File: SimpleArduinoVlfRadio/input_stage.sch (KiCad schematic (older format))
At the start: 0 parts

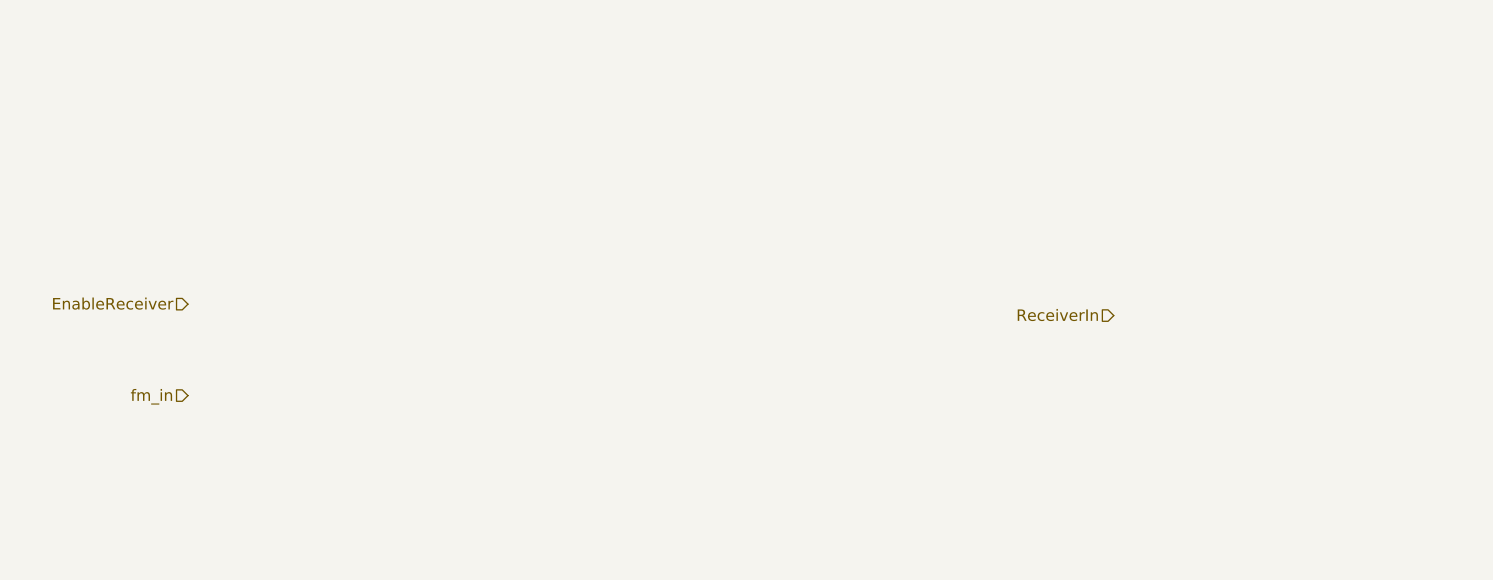
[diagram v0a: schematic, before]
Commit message: Updated Transmitter and finished fsk receiver
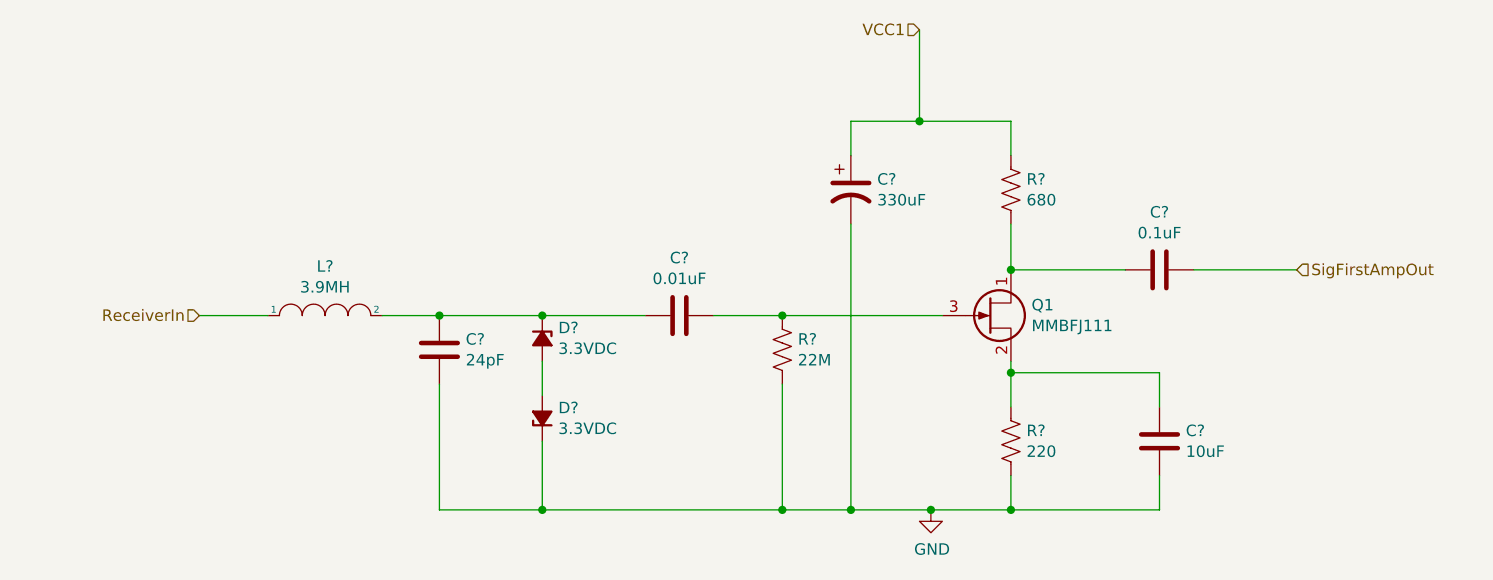
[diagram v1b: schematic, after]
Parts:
- added C?: 24pF, symbol Device:C
- added C?: 0.01uF, symbol Device:C
- added C?: 0.1uF, symbol Device:C
- added C?: 330uF, symbol Device:CP1
- added C?: 10uF, symbol Device:C
- added D? (x2): 3.3VDC, symbol Device:D_Zener_Small_ALT
- added L?: 3.9MH, symbol pspice:INDUCTOR
- added Q1: MMBFJ111, Package_TO_SOT_SMD:SOT-23, symbol Transistor_FET:MMBFJ111
- added R?: 22M, symbol Device:R_US
- added R?: 220, symbol Device:R_US
- added R?: 680, symbol Device:R_US
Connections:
- net ReceiverIn: now also L?.1
- new net: C?.2, Q1.1 (D), R?.2
- new net: C?.1, Q1.2 (S), R?.1
- new net: C?.1, Q1.3 (G), R?.1
- new net: C?.1, C?.2, D?.1 (K), L?.2
- new net: D?.2 (A), D?.2 (A)
- new net GND: C?.2, C?.2, C?.2, D?.1 (K), R?.2, R?.2
- new net SigFirstAmpOut: C?.1
- new net VCC1: C?.1, R?.1
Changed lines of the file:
@@
 $Descr A4 11693 8268
 encoding utf-8
-Sheet 5 10
+Sheet 7 14
 Title ""
 Date ""
@@
 Comment4 ""
 $EndDescr
-Text HLabel 2950 3100 0    50   Input ~ 0
-EnableReceiver
-Text HLabel 7000 3150 0    50   Input ~ 0
+Text HLabel 3000 3150 0    50   Input ~ 0
 ReceiverIn
-Text HLabel 2950 3500 0    50   Input ~ 0
-fm_in
+Text HLabel 7800 2950 2    50   Input ~ 0
+SigFirstAmpOut
+$Comp
+L Transistor_FET:MMBFJ111 Q1
+U 1 1 62A4F9A0
+P 6450 3150
+F 0 "Q1" H 6640 3196 50  0000 L CNN
+F 1 "MMBFJ111" H 6640 3105 50  0000 L CNN
+F 2 "Package_TO_SOT_SMD:SOT-23" H 6650 3075 50  0001 L CIN
+F 3 "https://www.onsemi.com/pub/Collateral/MMBFJ113-D.PDF" H 6450 3150 50  0001 L CNN
+	1    6450 3150
+	1    0    0    -1
+$EndComp
+$Comp
+L Device:D_Zener_Small_ALT D?
+U 1 1 62A51025
+P 4500 3250
+F 0 "D?" V 4454 3320 50  0000 L CNN
+F 1 "3.3VDC" V 4545 3320 50  0000 L CNN
+F 2 "" V 4500 3250 50  0001 C CNN
+F 3 "~" V 4500 3250 50  0001 C CNN
+	1    4500 3250
+	0    1    1    0
+$EndComp
+$Comp
+L Device:D_Zener_Small_ALT D?
+U 1 1 62A51E79
+P 4500 3600
+F 0 "D?" V 4546 3530 50  0000 R CNN
+F 1 "3.3VDC" V 4455 3530 50  0000 R CNN
+F 2 "" V 4500 3600 50  0001 C CNN
+F 3 "~" V 4500 3600 50  0001 C CNN
+	1    4500 3600
+	0    -1   -1   0
+$EndComp
+$Comp
+L Device:C C?
+U 1 1 62A52969
+P 4050 3300
+F 0 "C?" H 4165 3346 50  0000 L CNN
+F 1 "24pF" H 4165 3255 50  0000 L CNN
+F 2 "" H 4088 3150 50  0001 C CNN
+F 3 "~" H 4050 3300 50  0001 C CNN
+	1    4050 3300
+	1    0    0    -1
+$EndComp
+$Comp
+L pspice:INDUCTOR L?
+U 1 1 62A538F5
+P 3550 3150
+F 0 "L?" H 3550 3365 50  0000 C CNN
+F 1 "3.9MH" H 3550 3274 50  0000 C CNN
+F 2 "" H 3550 3150 50  0001 C CNN
+F 3 "~" H 3550 3150 50  0001 C CNN
+	1    3550 3150
+	1    0    0    -1
+$EndComp
+$Comp
+L Device:R_US R?
+U 1 1 62A55EF5
+P 5550 3300
+F 0 "R?" H 5618 3346 50  0000 L CNN
+F 1 "22M" H 5618 3255 50  0000 L CNN
+F 2 "" V 5590 3290 50  0001 C CNN
+F 3 "~" H 5550 3300 50  0001 C CNN
+	1    5550 3300
+	1    0    0    -1
+$EndComp
+$Comp
+L Device:R_US R?
+U 1 1 62A56EAC
+P 6550 3700
+F 0 "R?" H 6618 3746 50  0000 L CNN
+F 1 "220" H 6618 3655 50  0000 L CNN
+F 2 "" V 6590 3690 50  0001 C CNN
+F 3 "~" H 6550 3700 50  0001 C CNN
+	1    6550 3700
+	1    0    0    -1
+$EndComp
+$Comp
+L Device:R_US R?
+U 1 1 62A57945
+P 6550 2600
+F 0 "R?" H 6618 2646 50  0000 L CNN
+F 1 "680" H 6618 2555 50  0000 L CNN
+F 2 "" V 6590 2590 50  0001 C CNN
+F 3 "~" H 6550 2600 50  0001 C CNN
+	1    6550 2600
+	1    0    0    -1
+$EndComp
+$Comp
+L Device:C C?
+U 1 1 62A582F5
+P 5100 3150
+F 0 "C?" V 4848 3150 50  0000 C CNN
+F 1 "0.01uF" V 4939 3150 50  0000 C CNN
+F 2 "" H 5138 3000 50  0001 C CNN
+F 3 "~" H 5100 3150 50  0001 C CNN
+	1    5100 3150
+	0    1    1    0
+$EndComp
+$Comp
+L Device:C C?
+U 1 1 62A58A43
+P 7200 2950
+F 0 "C?" V 6948 2950 50  0000 C CNN
+F 1 "0.1uF" V 7039 2950 50  0000 C CNN
+F 2 "" H 7238 2800 50  0001 C CNN
+F 3 "~" H 7200 2950 50  0001 C CNN
+	1    7200 2950
+	0    1    1    0
+$EndComp
+$Comp
+L Device:CP1 C?
+U 1 1 62A5967F
+P 5850 2600
+F 0 "C?" H 5965 2646 50  0000 L CNN
+F 1 "330uF" H 5965 2555 50  0000 L CNN
+F 2 "" H 5850 2600 50  0001 C CNN
+F 3 "~" H 5850 2600 50  0001 C CNN
+	1    5850 2600
+	1    0    0    -1
+$EndComp
+$Comp
+L Device:C C?
+U 1 1 62A5ABDD
+P 7200 3700
+F 0 "C?" H 7315 3746 50  0000 L CNN
+F 1 "10uF" H 7315 3655 50  0000 L CNN
+F 2 "" H 7238 3550 50  0001 C CNN
+F 3 "~" H 7200 3700 50  0001 C CNN
+	1    7200 3700
+	1    0    0    -1
+$EndComp
+Wire Wire Line
+	3000 3150 3300 3150
+Wire Wire Line
+	3800 3150 4050 3150
+Wire Wire Line
+	4050 3150 4500 3150
+Connection ~ 4050 3150
+Wire Wire Line
+	4500 3350 4500 3500
+Wire Wire Line
+	4500 3150 4950 3150
+Connection ~ 4500 3150
+Wire Wire Line
+	5250 3150 5550 3150
+Wire Wire Line
+	6550 2950 6550 2750
+Wire Wire Line
+	6550 3350 6550 3400
+Wire Wire Line
+	6550 2450 6550 2300
+Wire Wire Line
+	6550 2300 6150 2300
+Wire Wire Line
+	5850 2300 5850 2450
+Wire Wire Line
+	7050 2950 6550 2950
+Connection ~ 6550 2950
+Wire Wire Line
+	7350 2950 7800 2950
+$Comp
+L power:GND #PWR?
+U 1 1 62A60847
+P 6200 4000
+F 0 "#PWR?" H 6200 3750 50  0001 C CNN
+F 1 "GND" H 6205 3827 50  0000 C CNN
+F 2 "" H 6200 4000 50  0001 C CNN
+F 3 "" H 6200 4000 50  0001 C CNN
+	1    6200 4000
+	1    0    0    -1
+$EndComp
+Text HLabel 6150 1900 0    50   Input ~ 0
+VCC1
+Wire Wire Line
+	6150 1900 6150 2300
+Connection ~ 6150 2300
+Wire Wire Line
+	6150 2300 5850 2300
+Wire Wire Line
+	5850 2750 5850 4000
+Wire Wire Line
+	5850 4000 6200 4000
+Connection ~ 5550 3150
+Wire Wire Line
+	5550 3150 6250 3150
+Wire Wire Line
+	6200 4000 6550 4000
+Wire Wire Line
+	6550 4000 6550 3850
+Connection ~ 6200 4000
+Wire Wire Line
+	6550 4000 7200 4000
+Wire Wire Line
+	7200 4000 7200 3850
+Connection ~ 6550 4000
+Wire Wire Line
+	7200 3550 7200 3400
+Wire Wire Line
+	7200 3400 6550 3400
+Connection ~ 6550 3400
+Wire Wire Line
+	6550 3400 6550 3550
+Wire Wire Line
+	5550 3450 5550 4000
+Wire Wire Line
+	5550 4000 5850 4000
+Connection ~ 5850 4000
+Wire Wire Line
+	4500 3700 4500 4000
+Wire Wire Line
+	4500 4000 5550 4000
+Connection ~ 5550 4000
+Wire Wire Line
+	4050 3450 4050 4000
+Wire Wire Line
+	4050 4000 4500 4000
+Connection ~ 4500 4000
 $EndSCHEMATC

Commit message: Fix misplaced zenier diodes
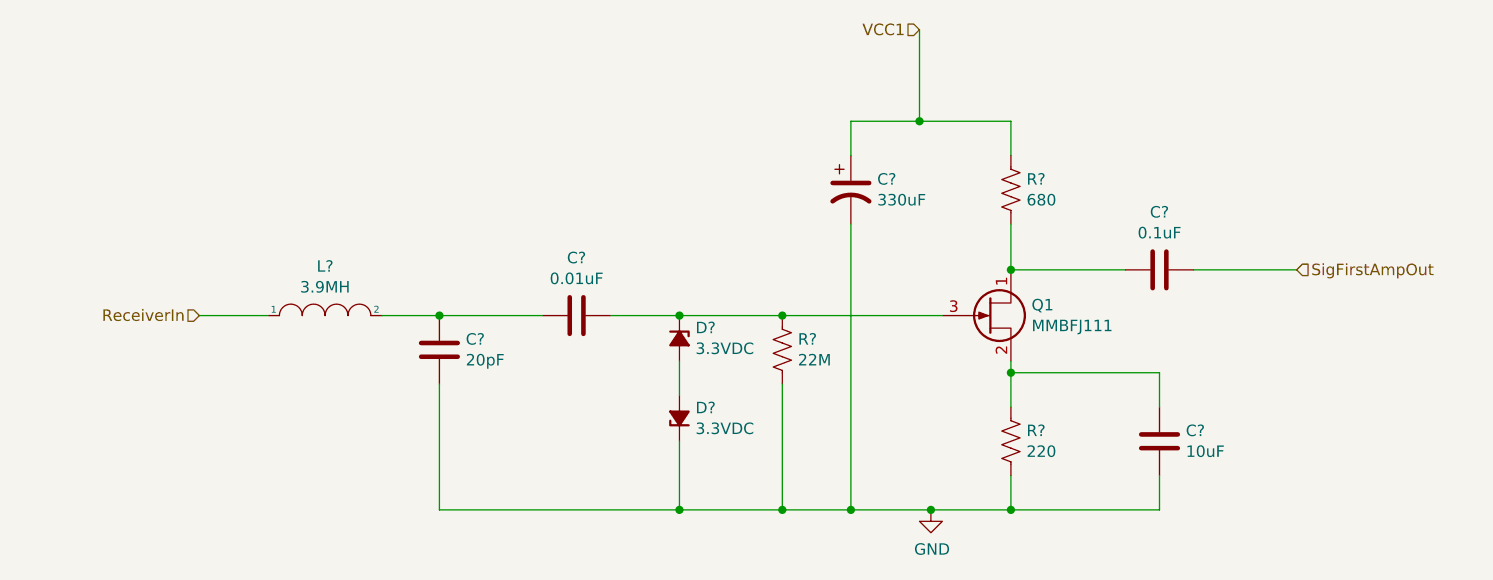
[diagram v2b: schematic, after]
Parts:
- C?: value 24pF -> 20pF
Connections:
- net at C?.1, Q1.3 (G), R?.1: now also D?.1 (K)
- net at C?.1, C?.2, L?.2: no longer D?.1 (K)
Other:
- moved on the sheet: C?, D?
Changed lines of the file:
@@
 L Device:D_Zener_Small_ALT D?
 U 1 1 62A51025
-P 4500 3250
-F 0 "D?" V 4454 3320 50  0000 L CNN
-F 1 "3.3VDC" V 4545 3320 50  0000 L CNN
-F 2 "" V 4500 3250 50  0001 C CNN
-F 3 "~" V 4500 3250 50  0001 C CNN
-	1    4500 3250
+P 5100 3250
+F 0 "D?" V 5054 3320 50  0000 L CNN
+F 1 "3.3VDC" V 5145 3320 50  0000 L CNN
+F 2 "" V 5100 3250 50  0001 C CNN
+F 3 "~" V 5100 3250 50  0001 C CNN
+	1    5100 3250
 	0    1    1    0
 $EndComp
@@
 L Device:D_Zener_Small_ALT D?
 U 1 1 62A51E79
-P 4500 3600
-F 0 "D?" V 4546 3530 50  0000 R CNN
-F 1 "3.3VDC" V 4455 3530 50  0000 R CNN
-F 2 "" V 4500 3600 50  0001 C CNN
-F 3 "~" V 4500 3600 50  0001 C CNN
-	1    4500 3600
+P 5100 3600
+F 0 "D?" V 5146 3530 50  0000 R CNN
+F 1 "3.3VDC" V 5055 3530 50  0000 R CNN
+F 2 "" V 5100 3600 50  0001 C CNN
+F 3 "~" V 5100 3600 50  0001 C CNN
+	1    5100 3600
 	0    -1   -1   0
 $EndComp
@@
 P 4050 3300
 F 0 "C?" H 4165 3346 50  0000 L CNN
-F 1 "24pF" H 4165 3255 50  0000 L CNN
+F 1 "20pF" H 4165 3255 50  0000 L CNN
 F 2 "" H 4088 3150 50  0001 C CNN
 F 3 "~" H 4050 3300 50  0001 C CNN
@@
 L Device:C C?
 U 1 1 62A582F5
-P 5100 3150
-F 0 "C?" V 4848 3150 50  0000 C CNN
-F 1 "0.01uF" V 4939 3150 50  0000 C CNN
-F 2 "" H 5138 3000 50  0001 C CNN
-F 3 "~" H 5100 3150 50  0001 C CNN
-	1    5100 3150
+P 4650 3150
+F 0 "C?" V 4398 3150 50  0000 C CNN
+F 1 "0.01uF" V 4489 3150 50  0000 C CNN
+F 2 "" H 4688 3000 50  0001 C CNN
+F 3 "~" H 4650 3150 50  0001 C CNN
+	1    4650 3150
 	0    1    1    0
 $EndComp
@@
 	3000 3150 3300 3150
 Wire Wire Line
-	3800 3150 4050 3150
-Wire Wire Line
-	4050 3150 4500 3150
-Connection ~ 4050 3150
-Wire Wire Line
-	4500 3350 4500 3500
-Wire Wire Line
-	4500 3150 4950 3150
-Connection ~ 4500 3150
-Wire Wire Line
-	5250 3150 5550 3150
+	5100 3350 5100 3500
 Wire Wire Line
 	6550 2950 6550 2750
@@
 Wire Wire Line
 	5850 4000 6200 4000
-Connection ~ 5550 3150
 Wire Wire Line
 	5550 3150 6250 3150
@@
 Connection ~ 5850 4000
 Wire Wire Line
-	4500 3700 4500 4000
-Wire Wire Line
-	4500 4000 5550 4000
+	5100 3700 5100 4000
 Connection ~ 5550 4000
 Wire Wire Line
 	4050 3450 4050 4000
 Wire Wire Line
-	4050 4000 4500 4000
-Connection ~ 4500 4000
+	4050 4000 5100 4000
+Connection ~ 5100 4000
+Wire Wire Line
+	5100 4000 5550 4000
+Wire Wire Line
+	3800 3150 4050 3150
+Connection ~ 4050 3150
+Wire Wire Line
+	4050 3150 4500 3150
+Wire Wire Line
+	4800 3150 5100 3150
+Wire Wire Line
+	5550 3150 5100 3150
+Connection ~ 5550 3150
+Connection ~ 5100 3150
 $EndSCHEMATC

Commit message: Fix resistor to match prototype
Match prototype instead of matching vlf-3
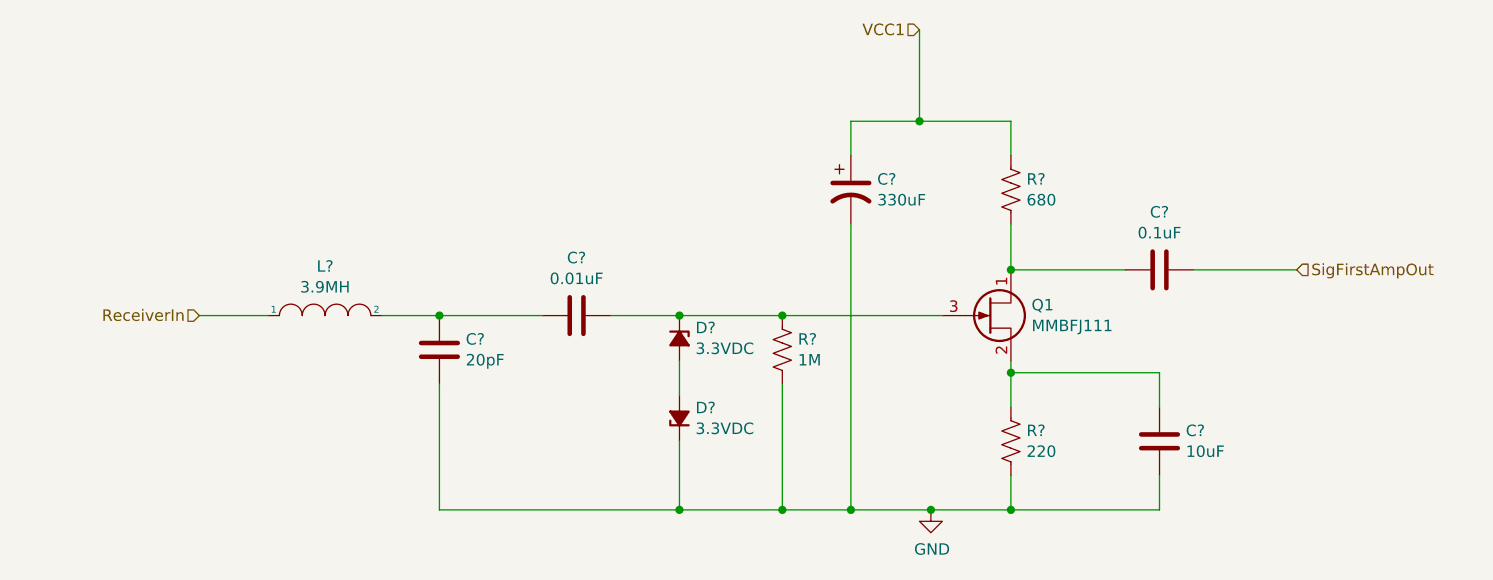
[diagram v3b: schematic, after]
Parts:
- R?: value 22M -> 1M
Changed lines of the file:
@@
 P 5550 3300
 F 0 "R?" H 5618 3346 50  0000 L CNN
-F 1 "22M" H 5618 3255 50  0000 L CNN
+F 1 "1M" H 5618 3255 50  0000 L CNN
 F 2 "" V 5590 3290 50  0001 C CNN
 F 3 "~" H 5550 3300 50  0001 C CNN
